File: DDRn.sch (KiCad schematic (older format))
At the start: 112 parts

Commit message: Creating the DDR template.
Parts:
- removed C? (x43): 0.1UF, symbol C
- removed R? (x2): R, symbol R
- removed R? (x5): 49.9E, ~, symbol RES_NET4
- removed R? (x2): 100E, symbol R
- removed R? (x3): 4K7, symbol R
- removed U?: MT41J128M16, ~, symbol MT41J128M16
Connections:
- net labels added: DDRn_A0, DDRn_A1, DDRn_A10, DDRn_A11, DDRn_A12, DDRn_A13, DDRn_A14, DDRn_A2, DDRn_A3, DDRn_A4, DDRn_A5, DDRn_A6, DDRn_A7, DDRn_A8, DDRn_A9, DDRn_A[0..14], DDRn_BA0, DDRn_BA1, DDRn_BA2, DDRn_BA[0..2], DDRn_CASN0, DDRn_CAS_N, DDRn_CKE, DDRn_CK_N, DDRn_CK_P, DDRn_CS_N, DDRn_DQ0, DDRn_DQ1, DDRn_DQ10, DDRn_DQ11, DDRn_DQ12, DDRn_DQ13, DDRn_DQ14, DDRn_DQ15, DDRn_DQ2, DDRn_DQ3, DDRn_DQ4, DDRn_DQ5, DDRn_DQ6, DDRn_DQ7, DDRn_DQ8, DDRn_DQ9, DDRn_DQ[0..15], DDRn_LDM, DDRn_LDQS_N, DDRn_LDQS_P, DDRn_ODT, DDRn_RASN0, DDRn_RAS_N, DDRn_RESET_N, DDRn_UDM, DDRn_UDQS_N, DDRn_UDQS_P, DDRn_WE0, DDRn_WE_N, DDRn_ZQ, VTTDDRn
- net labels removed: CASN, CASN0, DDR0_A0, DDR0_A1, DDR0_A10, DDR0_A11, DDR0_A12, DDR0_A13, DDR0_A14, DDR0_A2, DDR0_A3, DDR0_A4, DDR0_A5, DDR0_A6, DDR0_A7, DDR0_A8, DDR0_A9, DDR0_A[0..14], DDR0_BA0, DDR0_BA1, DDR0_BA2, DDR0_BA[0..2], DDR0_CAS_N, DDR0_CKE, DDR0_CK_N, DDR0_CK_P, DDR0_CS_N, DDR0_DQ0, DDR0_DQ1, DDR0_DQ10, DDR0_DQ11, DDR0_DQ12, DDR0_DQ13, DDR0_DQ14, DDR0_DQ15, DDR0_DQ2, DDR0_DQ3, DDR0_DQ4, DDR0_DQ5, DDR0_DQ6, DDR0_DQ7, DDR0_DQ8, DDR0_DQ9, DDR0_DQ[0..15], DDR0_LDM, DDR0_LDQS_N, DDR0_LDQS_P, DDR0_ODT, DDR0_RAS_N, DDR0_RESET_N, DDR0_UDM, DDR0_UDQS_N, DDR0_UDQS_P, DDR0_WE_N, DDR0_ZQ, DDR1_A0, DDR1_A1, DDR1_A10, DDR1_A11, DDR1_A12, DDR1_A13, DDR1_A14, DDR1_A2, DDR1_A3, DDR1_A4, DDR1_A5, DDR1_A6, DDR1_A7, DDR1_A8, DDR1_A9, DDR1_A[0..14], DDR1_BA0, DDR1_BA1, DDR1_BA2, DDR1_BA[0..2], DDR1_CAS_N, DDR1_CKE, DDR1_CK_N, DDR1_CK_P, DDR1_CS_N, DDR1_DQ0, DDR1_DQ1, DDR1_DQ10, DDR1_DQ11, DDR1_DQ12, DDR1_DQ13, DDR1_DQ14, DDR1_DQ15, DDR1_DQ2, DDR1_DQ3, DDR1_DQ4, DDR1_DQ5, DDR1_DQ6, DDR1_DQ7, DDR1_DQ8, DDR1_DQ9, DDR1_DQ[0..15], DDR1_LDM, DDR1_LDQS_N, DDR1_LDQS_P, DDR1_ODT, DDR1_RAS_N, DDR1_RESET_N, DDR1_UDM, DDR1_UDQS_N, DDR1_UDQS_P, DDR1_WE_N, DDR1_ZQ, RASN, RASN0, VTTDDR0, VTTDDR1, VTTREF1, WE0, WEN
- wire segments 406 -> 363
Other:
- moved on the sheet: C?, R?

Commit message: Fix minor connections
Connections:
- wire segments 363 -> 362
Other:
- moved on the sheet: C?

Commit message: Adding DDRn name to resistor/capacitors.
s/R?/RDDRn?/
s/C?/CDDRn?/
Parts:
- gave numbers to parts that had none: 2

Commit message: s/U1/UDDRn1/
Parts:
- gave numbers to parts that had none: 1
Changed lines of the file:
@@
 $EndDescr
 $Comp
-L MT41J128M16 U?
+L MT41J128M16 UDDRn1
 U 1 1 57C61740
 P 8400 5050
-F 0 "U?" H 8350 7900 60  0000 C CNN
+F 0 "UDDRn1" H 8350 7900 60  0000 C CNN
 F 1 "MT41J128M16" H 8350 1500 60  0000 C CNN
 F 2 "~" H 8400 5050 60  0000 C CNN

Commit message: Annotate the schematic.
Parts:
- gave numbers to parts that had none: 55

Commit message: s/DDRn/$DDRn$/gc
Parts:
- renumbered CDDRn1 to C$DDRn$1, CDDRn10 to C$DDRn$10, CDDRn11 to C$DDRn$11, CDDRn12 to C$DDRn$12, CDDRn13 to C$DDRn$13, CDDRn14 to C$DDRn$14, CDDRn15 to C$DDRn$15, CDDRn16 to C$DDRn$16, CDDRn17 to C$DDRn$17, CDDRn18 to C$DDRn$18, CDDRn19 to C$DDRn$19, CDDRn2 to C$DDRn$2, CDDRn20 to C$DDRn$20, CDDRn21 to C$DDRn$21, CDDRn22 to C$DDRn$22, CDDRn23 to C$DDRn$23, CDDRn24 to C$DDRn$24, CDDRn25 to C$DDRn$25, CDDRn26 to C$DDRn$26, CDDRn27 to C$DDRn$27, CDDRn28 to C$DDRn$28, CDDRn29 to C$DDRn$29, CDDRn3 to C$DDRn$3, CDDRn30 to C$DDRn$30, CDDRn31 to C$DDRn$31, CDDRn32 to C$DDRn$32, CDDRn33 to C$DDRn$33, CDDRn34 to C$DDRn$34, CDDRn35 to C$DDRn$35, CDDRn36 to C$DDRn$36, CDDRn37 to C$DDRn$37, CDDRn38 to C$DDRn$38, CDDRn39 to C$DDRn$39, CDDRn4 to C$DDRn$4, CDDRn40 to C$DDRn$40, CDDRn41 to C$DDRn$41, CDDRn42 to C$DDRn$42, CDDRn43 to C$DDRn$43, CDDRn5 to C$DDRn$5, CDDRn6 to C$DDRn$6, CDDRn7 to C$DDRn$7, CDDRn8 to C$DDRn$8, CDDRn9 to C$DDRn$9, RDDRn1 to R$DDRn$1, RDDRn10 to R$DDRn$10, RDDRn11 to R$DDRn$11, RDDRn12 to R$DDRn$12, RDDRn2 to R$DDRn$2, RDDRn3 to R$DDRn$3, RDDRn4 to R$DDRn$4, RDDRn5 to R$DDRn$5, RDDRn6 to R$DDRn$6, RDDRn7 to R$DDRn$7, RDDRn8 to R$DDRn$8, RDDRn9 to R$DDRn$9, UDDRn1 to U$DDRn$1
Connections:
- net labels added: $DDRn$_A0, $DDRn$_A1, $DDRn$_A10, $DDRn$_A11, $DDRn$_A12, $DDRn$_A13, $DDRn$_A14, $DDRn$_A2, $DDRn$_A3, $DDRn$_A4, $DDRn$_A5, $DDRn$_A6, $DDRn$_A7, $DDRn$_A8, $DDRn$_A9, $DDRn$_A[0..14], $DDRn$_BA0, $DDRn$_BA1, $DDRn$_BA2, $DDRn$_BA[0..2], $DDRn$_CASN0, $DDRn$_CAS_N, $DDRn$_CKE, $DDRn$_CK_N, $DDRn$_CK_P, $DDRn$_CS_N, $DDRn$_DQ0, $DDRn$_DQ1, $DDRn$_DQ10, $DDRn$_DQ11, $DDRn$_DQ12, $DDRn$_DQ13, $DDRn$_DQ14, $DDRn$_DQ15, $DDRn$_DQ2, $DDRn$_DQ3, $DDRn$_DQ4, $DDRn$_DQ5, $DDRn$_DQ6, $DDRn$_DQ7, $DDRn$_DQ8, $DDRn$_DQ9, $DDRn$_DQ[0..15], $DDRn$_LDM, $DDRn$_LDQS_N, $DDRn$_LDQS_P, $DDRn$_ODT, $DDRn$_RASN0, $DDRn$_RAS_N, $DDRn$_RESET_N, $DDRn$_UDM, $DDRn$_UDQS_N, $DDRn$_UDQS_P, $DDRn$_WE0, $DDRn$_WE_N, $DDRn$_ZQ, VTT$DDRn$
- net labels removed: DDRn_A0, DDRn_A1, DDRn_A10, DDRn_A11, DDRn_A12, DDRn_A13, DDRn_A14, DDRn_A2, DDRn_A3, DDRn_A4, DDRn_A5, DDRn_A6, DDRn_A7, DDRn_A8, DDRn_A9, DDRn_A[0..14], DDRn_BA0, DDRn_BA1, DDRn_BA2, DDRn_BA[0..2], DDRn_CASN0, DDRn_CAS_N, DDRn_CKE, DDRn_CK_N, DDRn_CK_P, DDRn_CS_N, DDRn_DQ0, DDRn_DQ1, DDRn_DQ10, DDRn_DQ11, DDRn_DQ12, DDRn_DQ13, DDRn_DQ14, DDRn_DQ15, DDRn_DQ2, DDRn_DQ3, DDRn_DQ4, DDRn_DQ5, DDRn_DQ6, DDRn_DQ7, DDRn_DQ8, DDRn_DQ9, DDRn_DQ[0..15], DDRn_LDM, DDRn_LDQS_N, DDRn_LDQS_P, DDRn_ODT, DDRn_RASN0, DDRn_RAS_N, DDRn_RESET_N, DDRn_UDM, DDRn_UDQS_N, DDRn_UDQS_P, DDRn_WE0, DDRn_WE_N, DDRn_ZQ, VTTDDRn

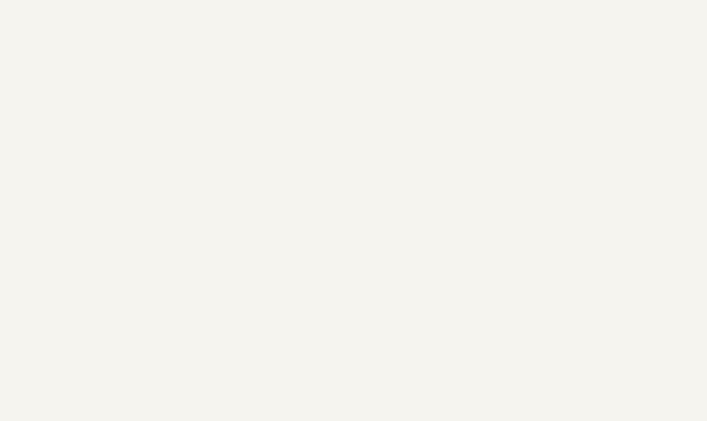
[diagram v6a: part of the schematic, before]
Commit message: Adding warning text.
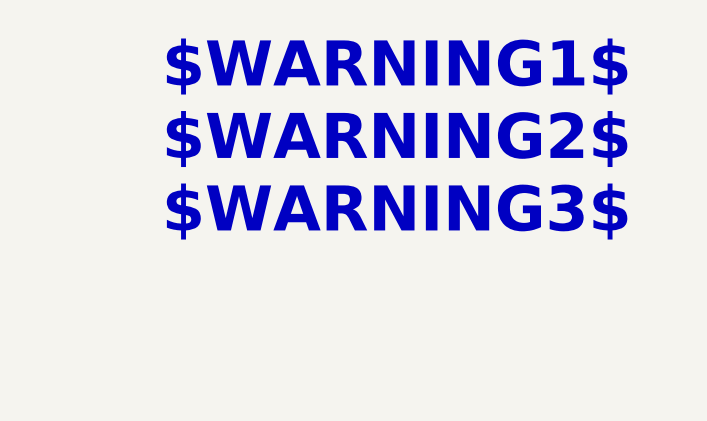
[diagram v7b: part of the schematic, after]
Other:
- note added: "$WARNING1$\n$WARNING2$\n$WARNING3$"
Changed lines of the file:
@@
 LIBS:hdmi2usb
 LIBS:HDMI2USB-cache
+LIBS:DDRn-cache
 EELAYER 25 0
 EELAYER END
@@
 Wire Wire Line
 	2500 10775 2500 10700
+Text Notes 11780 2715 0    197  ~ 39
+$WARNING1$\n$WARNING2$\n$WARNING3$
 $EndSCHEMATC

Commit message: s/UF/uF/gc
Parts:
- C$DDRn$1, C$DDRn$10, C$DDRn$11, C$DDRn$12, C$DDRn$13, C$DDRn$14, C$DDRn$15, C$DDRn$16, C$DDRn$17, C$DDRn$18, C$DDRn$19, C$DDRn$2, C$DDRn$20, C$DDRn$21, C$DDRn$22, C$DDRn$23, C$DDRn$24, C$DDRn$25, C$DDRn$26, C$DDRn$27, C$DDRn$28, C$DDRn$29, C$DDRn$3, C$DDRn$30, C$DDRn$31, C$DDRn$32, C$DDRn$33, C$DDRn$34, C$DDRn$35, C$DDRn$36, C$DDRn$37, C$DDRn$38, C$DDRn$39, C$DDRn$4, C$DDRn$40, C$DDRn$41, C$DDRn$42, C$DDRn$43, C$DDRn$5, C$DDRn$6, C$DDRn$7, C$DDRn$8, C$DDRn$9: value 0.1UF -> 0.1uF
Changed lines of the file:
@@
 P 9500 4950
 F 0 "C$DDRn$43" H 9550 5050 50  0000 L CNN
-F 1 "0.1UF" H 9550 4850 50  0000 L CNN
+F 1 "0.1uF" H 9550 4850 50  0000 L CNN
 F 2 "" H 9500 4950 60  0000 C CNN
 F 3 "" H 9500 4950 60  0000 C CNN
@@
 P 2250 13650
 F 0 "C$DDRn$3" H 2300 13750 50  0000 L CNN
-F 1 "0.1UF" H 2300 13550 50  0000 L CNN
+F 1 "0.1uF" H 2300 13550 50  0000 L CNN
 F 2 "" H 2250 13650 60  0000 C CNN
 F 3 "" H 2250 13650 60  0000 C CNN
@@
 P 2600 13650
 F 0 "C$DDRn$6" H 2650 13750 50  0000 L CNN
-F 1 "0.1UF" H 2650 13550 50  0000 L CNN
+F 1 "0.1uF" H 2650 13550 50  0000 L CNN
 F 2 "" H 2600 13650 60  0000 C CNN
 F 3 "" H 2600 13650 60  0000 C CNN
@@
 P 3000 13650
 F 0 "C$DDRn$9" H 3050 13750 50  0000 L CNN
-F 1 "0.1UF" H 3050 13550 50  0000 L CNN
+F 1 "0.1uF" H 3050 13550 50  0000 L CNN
 F 2 "" H 3000 13650 60  0000 C CNN
 F 3 "" H 3000 13650 60  0000 C CNN
@@
 P 3400 13650
 F 0 "C$DDRn$12" H 3450 13750 50  0000 L CNN
-F 1 "0.1UF" H 3450 13550 50  0000 L CNN
+F 1 "0.1uF" H 3450 13550 50  0000 L CNN
 F 2 "" H 3400 13650 60  0000 C CNN
 F 3 "" H 3400 13650 60  0000 C CNN
@@
 P 3750 13650
 F 0 "C$DDRn$16" H 3800 13750 50  0000 L CNN
-F 1 "0.1UF" H 3800 13550 50  0000 L CNN
+F 1 "0.1uF" H 3800 13550 50  0000 L CNN
 F 2 "" H 3750 13650 60  0000 C CNN
 F 3 "" H 3750 13650 60  0000 C CNN
@@
 P 4100 13650
 F 0 "C$DDRn$19" H 4150 13750 50  0000 L CNN
-F 1 "0.1UF" H 4150 13550 50  0000 L CNN
+F 1 "0.1uF" H 4150 13550 50  0000 L CNN
 F 2 "" H 4100 13650 60  0000 C CNN
 F 3 "" H 4100 13650 60  0000 C CNN
@@
 P 4550 13650
 F 0 "C$DDRn$22" H 4600 13750 50  0000 L CNN
-F 1 "0.1UF" H 4600 13550 50  0000 L CNN
+F 1 "0.1uF" H 4600 13550 50  0000 L CNN
 F 2 "" H 4550 13650 60  0000 C CNN
 F 3 "" H 4550 13650 60  0000 C CNN
@@
 P 4950 13650
 F 0 "C$DDRn$25" H 5000 13750 50  0000 L CNN
-F 1 "0.1UF" H 5000 13550 50  0000 L CNN
+F 1 "0.1uF" H 5000 13550 50  0000 L CNN
 F 2 "" H 4950 13650 60  0000 C CNN
 F 3 "" H 4950 13650 60  0000 C CNN
@@
 P 5350 13650
 F 0 "C$DDRn$28" H 5400 13750 50  0000 L CNN
-F 1 "0.1UF" H 5400 13550 50  0000 L CNN
+F 1 "0.1uF" H 5400 13550 50  0000 L CNN
 F 2 "" H 5350 13650 60  0000 C CNN
 F 3 "" H 5350 13650 60  0000 C CNN
@@
 P 5700 13650
 F 0 "C$DDRn$30" H 5750 13750 50  0000 L CNN
-F 1 "0.1UF" H 5750 13550 50  0000 L CNN
+F 1 "0.1uF" H 5750 13550 50  0000 L CNN
 F 2 "" H 5700 13650 60  0000 C CNN
 F 3 "" H 5700 13650 60  0000 C CNN
@@
 P 6150 13650
 F 0 "C$DDRn$32" H 6200 13750 50  0000 L CNN
-F 1 "0.1UF" H 6200 13550 50  0000 L CNN
+F 1 "0.1uF" H 6200 13550 50  0000 L CNN
 F 2 "" H 6150 13650 60  0000 C CNN
 F 3 "" H 6150 13650 60  0000 C CNN
@@
 P 6600 13650
 F 0 "C$DDRn$34" H 6650 13750 50  0000 L CNN
-F 1 "0.1UF" H 6650 13550 50  0000 L CNN
+F 1 "0.1uF" H 6650 13550 50  0000 L CNN
 F 2 "" H 6600 13650 60  0000 C CNN
 F 3 "" H 6600 13650 60  0000 C CNN
@@
 P 7000 13650
 F 0 "C$DDRn$36" H 7050 13750 50  0000 L CNN
-F 1 "0.1UF" H 7050 13550 50  0000 L CNN
+F 1 "0.1uF" H 7050 13550 50  0000 L CNN
 F 2 "" H 7000 13650 60  0000 C CNN
 F 3 "" H 7000 13650 60  0000 C CNN
@@
 P 7400 13650
 F 0 "C$DDRn$38" H 7450 13750 50  0000 L CNN
-F 1 "0.1UF" H 7450 13550 50  0000 L CNN
+F 1 "0.1uF" H 7450 13550 50  0000 L CNN
 F 2 "" H 7400 13650 60  0000 C CNN
 F 3 "" H 7400 13650 60  0000 C CNN
@@
 P 7800 13650
 F 0 "C$DDRn$40" H 7850 13750 50  0000 L CNN
-F 1 "0.1UF" H 7850 13550 50  0000 L CNN
+F 1 "0.1uF" H 7850 13550 50  0000 L CNN
 F 2 "" H 7800 13650 60  0000 C CNN
 F 3 "" H 7800 13650 60  0000 C CNN
@@
 P 2250 13150
 F 0 "C$DDRn$2" H 2300 13250 50  0000 L CNN
-F 1 "0.1UF" H 2300 13050 50  0000 L CNN
+F 1 "0.1uF" H 2300 13050 50  0000 L CNN
 F 2 "" H 2250 13150 60  0000 C CNN
 F 3 "" H 2250 13150 60  0000 C CNN
@@
 P 2600 13150
 F 0 "C$DDRn$5" H 2650 13250 50  0000 L CNN
-F 1 "0.1UF" H 2650 13050 50  0000 L CNN
+F 1 "0.1uF" H 2650 13050 50  0000 L CNN
 F 2 "" H 2600 13150 60  0000 C CNN
 F 3 "" H 2600 13150 60  0000 C CNN
@@
 P 3000 13150
 F 0 "C$DDRn$8" H 3050 13250 50  0000 L CNN
-F 1 "0.1UF" H 3050 13050 50  0000 L CNN
+F 1 "0.1uF" H 3050 13050 50  0000 L CNN
 F 2 "" H 3000 13150 60  0000 C CNN
 F 3 "" H 3000 13150 60  0000 C CNN
@@
 P 3400 13150
 F 0 "C$DDRn$11" H 3450 13250 50  0000 L CNN
-F 1 "0.1UF" H 3450 13050 50  0000 L CNN
+F 1 "0.1uF" H 3450 13050 50  0000 L CNN
 F 2 "" H 3400 13150 60  0000 C CNN
 F 3 "" H 3400 13150 60  0000 C CNN
@@
 P 3750 13150
 F 0 "C$DDRn$15" H 3800 13250 50  0000 L CNN
-F 1 "0.1UF" H 3800 13050 50  0000 L CNN
+F 1 "0.1uF" H 3800 13050 50  0000 L CNN
 F 2 "" H 3750 13150 60  0000 C CNN
 F 3 "" H 3750 13150 60  0000 C CNN
@@
 P 4100 13150
 F 0 "C$DDRn$18" H 4150 13250 50  0000 L CNN
-F 1 "0.1UF" H 4150 13050 50  0000 L CNN
+F 1 "0.1uF" H 4150 13050 50  0000 L CNN
 F 2 "" H 4100 13150 60  0000 C CNN
 F 3 "" H 4100 13150 60  0000 C CNN
@@
 P 4550 13150
 F 0 "C$DDRn$21" H 4600 13250 50  0000 L CNN
-F 1 "0.1UF" H 4600 13050 50  0000 L CNN
+F 1 "0.1uF" H 4600 13050 50  0000 L CNN
 F 2 "" H 4550 13150 60  0000 C CNN
 F 3 "" H 4550 13150 60  0000 C CNN
@@
 P 4950 13150
 F 0 "C$DDRn$24" H 5000 13250 50  0000 L CNN
-F 1 "0.1UF" H 5000 13050 50  0000 L CNN
+F 1 "0.1uF" H 5000 13050 50  0000 L CNN
 F 2 "" H 4950 13150 60  0000 C CNN
 F 3 "" H 4950 13150 60  0000 C CNN
@@
 P 5350 13150
 F 0 "C$DDRn$27" H 5400 13250 50  0000 L CNN
-F 1 "0.1UF" H 5400 13050 50  0000 L CNN
+F 1 "0.1uF" H 5400 13050 50  0000 L CNN
 F 2 "" H 5350 13150 60  0000 C CNN
 F 3 "" H 5350 13150 60  0000 C CNN
@@
 P 5700 13150
 F 0 "C$DDRn$29" H 5750 13250 50  0000 L CNN
-F 1 "0.1UF" H 5750 13050 50  0000 L CNN
+F 1 "0.1uF" H 5750 13050 50  0000 L CNN
 F 2 "" H 5700 13150 60  0000 C CNN
 F 3 "" H 5700 13150 60  0000 C CNN
@@
 P 6150 13150
 F 0 "C$DDRn$31" H 6200 13250 50  0000 L CNN
-F 1 "0.1UF" H 6200 13050 50  0000 L CNN
+F 1 "0.1uF" H 6200 13050 50  0000 L CNN
 F 2 "" H 6150 13150 60  0000 C CNN
 F 3 "" H 6150 13150 60  0000 C CNN
@@
 P 6600 13150
 F 0 "C$DDRn$33" H 6650 13250 50  0000 L CNN
-F 1 "0.1UF" H 6650 13050 50  0000 L CNN
+F 1 "0.1uF" H 6650 13050 50  0000 L CNN
 F 2 "" H 6600 13150 60  0000 C CNN
 F 3 "" H 6600 13150 60  0000 C CNN
@@
 P 7000 13150
 F 0 "C$DDRn$35" H 7050 13250 50  0000 L CNN
-F 1 "0.1UF" H 7050 13050 50  0000 L CNN
+F 1 "0.1uF" H 7050 13050 50  0000 L CNN
 F 2 "" H 7000 13150 60  0000 C CNN
 F 3 "" H 7000 13150 60  0000 C CNN
@@
 P 7400 13150
 F 0 "C$DDRn$37" H 7450 13250 50  0000 L CNN
-F 1 "0.1UF" H 7450 13050 50  0000 L CNN
+F 1 "0.1uF" H 7450 13050 50  0000 L CNN
 F 2 "" H 7400 13150 60  0000 C CNN
 F 3 "" H 7400 13150 60  0000 C CNN
@@
 P 7800 13150
 F 0 "C$DDRn$39" H 7850 13250 50  0000 L CNN
-F 1 "0.1UF" H 7850 13050 50  0000 L CNN
+F 1 "0.1uF" H 7850 13050 50  0000 L CNN
 F 2 "" H 7800 13150 60  0000 C CNN
 F 3 "" H 7800 13150 60  0000 C CNN
@@
 P 8100 13150
 F 0 "C$DDRn$41" H 8150 13250 50  0000 L CNN
-F 1 "0.1UF" H 8150 13050 50  0000 L CNN
+F 1 "0.1uF" H 8150 13050 50  0000 L CNN
 F 2 "" H 8100 13150 60  0000 C CNN
 F 3 "" H 8100 13150 60  0000 C CNN
@@
 P 8400 13150
 F 0 "C$DDRn$42" H 8450 13250 50  0000 L CNN
-F 1 "0.1UF" H 8450 13050 50  0000 L CNN
+F 1 "0.1uF" H 8450 13050 50  0000 L CNN
 F 2 "" H 8400 13150 60  0000 C CNN
 F 3 "" H 8400 13150 60  0000 C CNN
@@
 P 2230 14695
 F 0 "C$DDRn$1" H 2280 14795 50  0000 L CNN
-F 1 "0.1UF" H 2280 14595 50  0000 L CNN
+F 1 "0.1uF" H 2280 14595 50  0000 L CNN
 F 2 "" H 2230 14695 60  0000 C CNN
 F 3 "" H 2230 14695 60  0000 C CNN
@@
 P 2530 14695
 F 0 "C$DDRn$4" H 2580 14795 50  0000 L CNN
-F 1 "0.1UF" H 2580 14595 50  0000 L CNN
+F 1 "0.1uF" H 2580 14595 50  0000 L CNN
 F 2 "" H 2530 14695 60  0000 C CNN
 F 3 "" H 2530 14695 60  0000 C CNN
@@
 P 2830 14695
 F 0 "C$DDRn$7" H 2880 14795 50  0000 L CNN
-F 1 "0.1UF" H 2880 14595 50  0000 L CNN
+F 1 "0.1uF" H 2880 14595 50  0000 L CNN
 F 2 "" H 2830 14695 60  0000 C CNN
 F 3 "" H 2830 14695 60  0000 C CNN
@@
 P 3130 14695
 F 0 "C$DDRn$10" H 3180 14795 50  0000 L CNN
-F 1 "0.1UF" H 3180 14595 50  0000 L CNN
+F 1 "0.1uF" H 3180 14595 50  0000 L CNN
 F 2 "" H 3130 14695 60  0000 C CNN
 F 3 "" H 3130 14695 60  0000 C CNN
@@
 P 3430 14695
 F 0 "C$DDRn$13" H 3480 14795 50  0000 L CNN
-F 1 "0.1UF" H 3480 14595 50  0000 L CNN
+F 1 "0.1uF" H 3480 14595 50  0000 L CNN
 F 2 "" H 3430 14695 60  0000 C CNN
 F 3 "" H 3430 14695 60  0000 C CNN
@@
 P 3730 14695
 F 0 "C$DDRn$14" H 3780 14795 50  0000 L CNN
-F 1 "0.1UF" H 3780 14595 50  0000 L CNN
+F 1 "0.1uF" H 3780 14595 50  0000 L CNN
 F 2 "" H 3730 14695 60  0000 C CNN
 F 3 "" H 3730 14695 60  0000 C CNN
@@
 P 4030 14695
 F 0 "C$DDRn$17" H 4080 14795 50  0000 L CNN
-F 1 "0.1UF" H 4080 14595 50  0000 L CNN
+F 1 "0.1uF" H 4080 14595 50  0000 L CNN
 F 2 "" H 4030 14695 60  0000 C CNN
 F 3 "" H 4030 14695 60  0000 C CNN
@@
 P 4380 14695
 F 0 "C$DDRn$20" H 4430 14795 50  0000 L CNN
-F 1 "0.1UF" H 4430 14595 50  0000 L CNN
+F 1 "0.1uF" H 4430 14595 50  0000 L CNN
 F 2 "" H 4380 14695 60  0000 C CNN
 F 3 "" H 4380 14695 60  0000 C CNN
@@
 P 4680 14695
 F 0 "C$DDRn$23" H 4730 14795 50  0000 L CNN
-F 1 "0.1UF" H 4730 14595 50  0000 L CNN
+F 1 "0.1uF" H 4730 14595 50  0000 L CNN
 F 2 "" H 4680 14695 60  0000 C CNN
 F 3 "" H 4680 14695 60  0000 C CNN
@@
 P 4980 14695
 F 0 "C$DDRn$26" H 5030 14795 50  0000 L CNN
-F 1 "0.1UF" H 5030 14595 50  0000 L CNN
+F 1 "0.1uF" H 5030 14595 50  0000 L CNN
 F 2 "" H 4980 14695 60  0000 C CNN
 F 3 "" H 4980 14695 60  0000 C CNN
